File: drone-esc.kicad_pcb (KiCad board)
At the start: 4 copper layers, 34 x 34 mm, 249 parts, among them J1 SM08B-SRSS-TB_LF__SN_, Q1 IRLHS6242, Q10 IRLHS6242, Q11 IRLHS6242, Q12 IRLHS6242, Q13 IRLHS6242, Q14 IRLHS6242, Q15 IRLHS6242, Q16 IRLHS6242, Q17 IRLHS6242, Q18 IRLHS6242, Q19 IRLHS6242, Q2 IRLHS6242, Q20 IRLHS6242, Q21 IRLHS6242, Q22 IRLHS6242, Q23 IRLHS6242, Q24 IRLHS6242, Q3 IRLHS6242, Q4 IRLHS6242, Q5 IRLHS6242, Q6 IRLHS6242, Q7 IRLHS6242, Q8 IRLHS6242, Q9 IRLHS6242, U10 DGD05473FNQ-7, U11 DGD05473FNQ-7, U12 AT32F421G8U7, U13 DGD05473FNQ-7, U14 DGD05473FNQ-7, U15 DGD05473FNQ-7, U16 AT32F421G8U7, U17 DGD05473FNQ-7, U18 DGD05473FNQ-7, U19 DGD05473FNQ-7, U2 INA186A3IDCKR, U20 AT32F421G8U7, U3 TLV76733DRVR, U4 TPS61023DRLR, U5 AT32F421G8U7, U6 DGD05473FNQ-7, U7 DGD05473FNQ-7, U8 DGD05473FNQ-7, U9 DGD05473FNQ-7

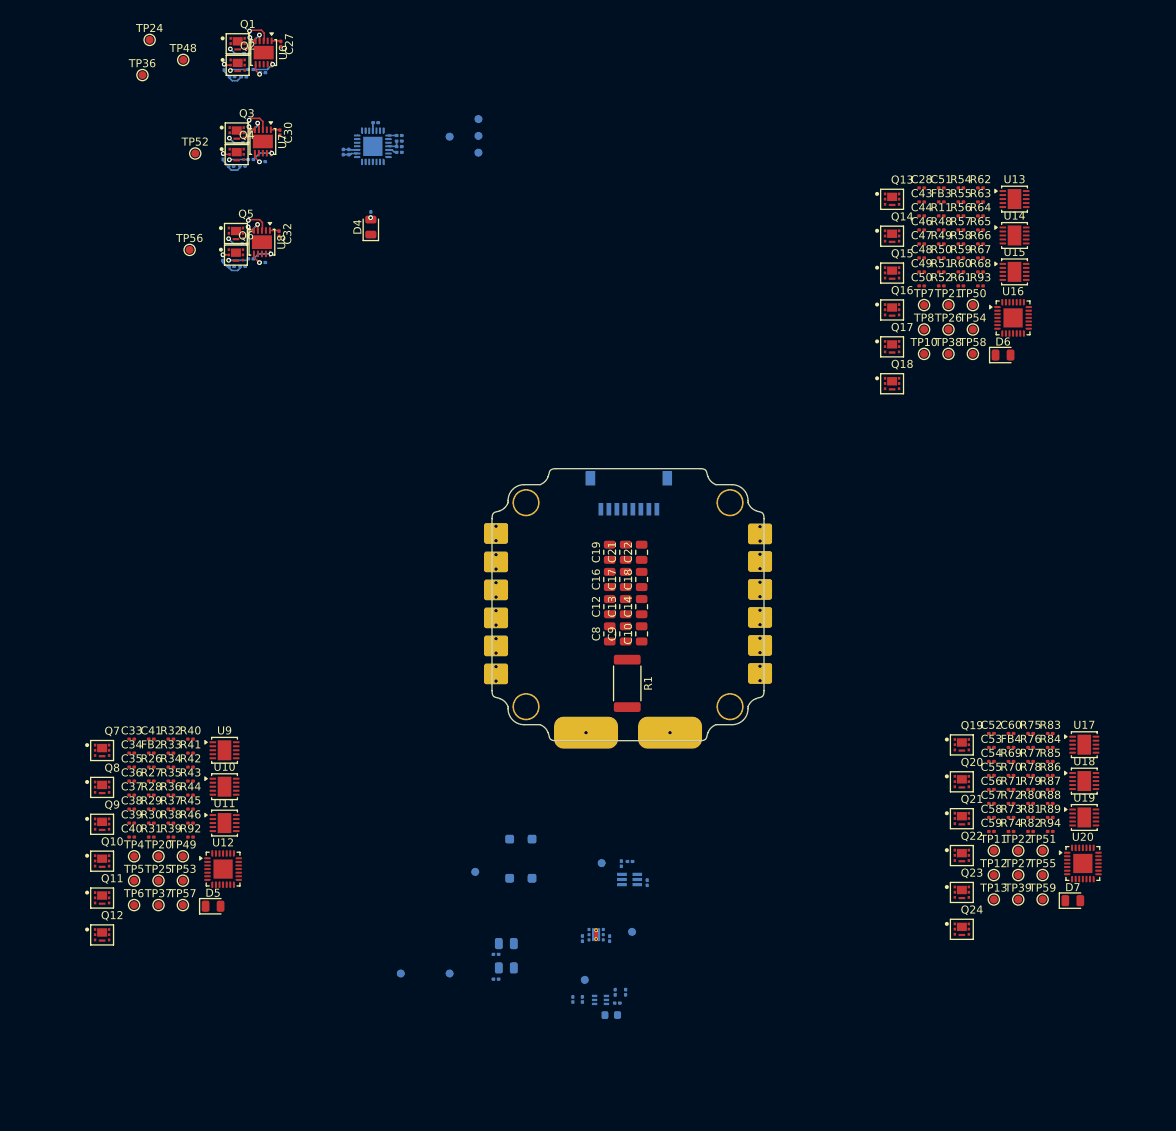
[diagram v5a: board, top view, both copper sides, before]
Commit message: duplicate layout and group
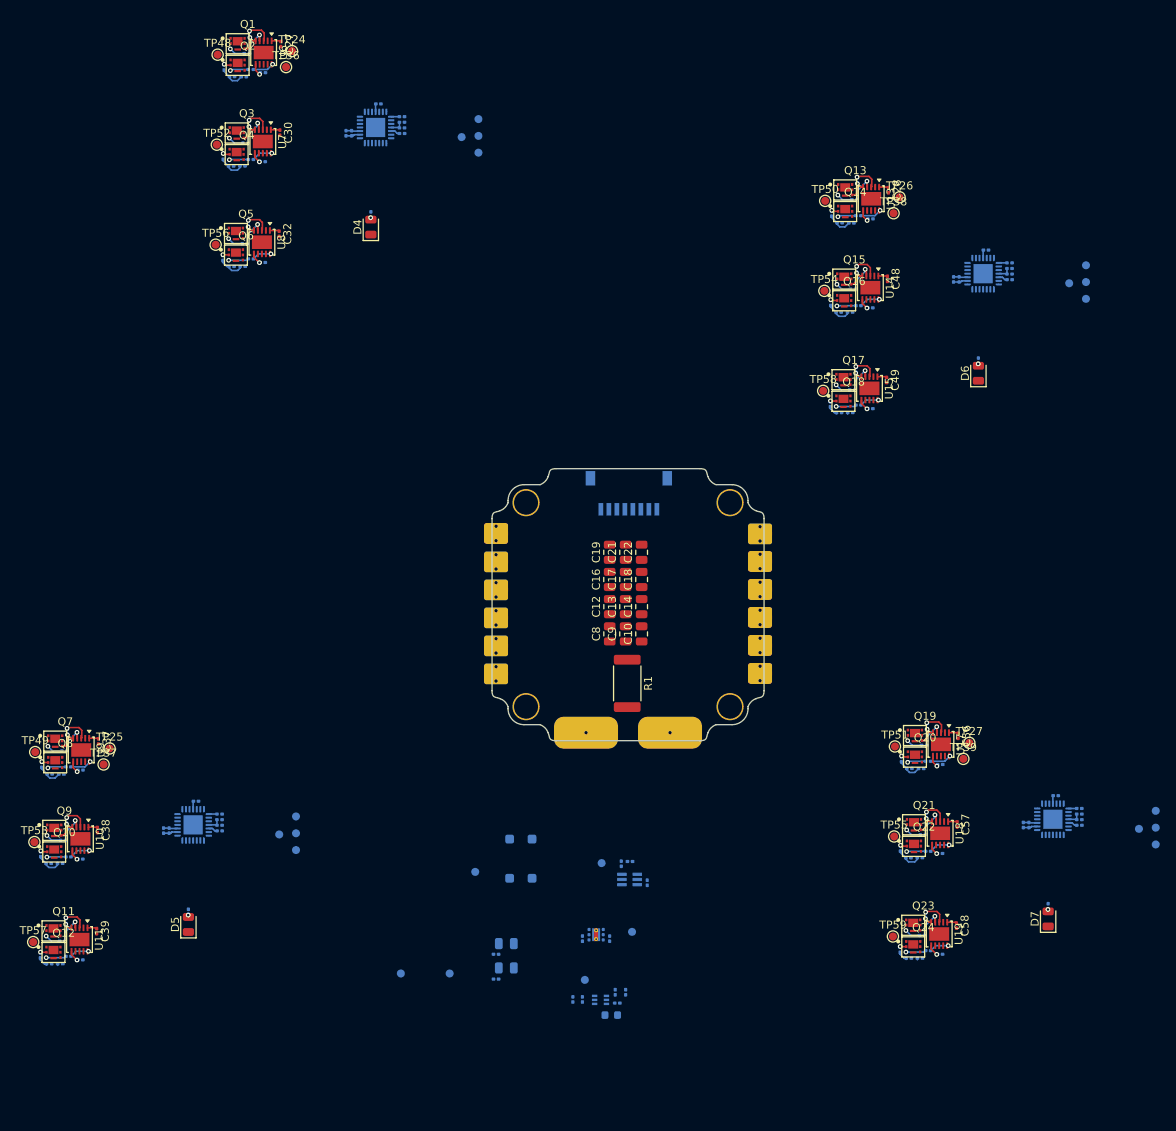
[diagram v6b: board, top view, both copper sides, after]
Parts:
- C33, C34, C35, C36, C40, C41, C43, C44, C46, C47, C50, C51, C52, C53, C54, C55, C59, C60, FB2, FB3, FB4, R11, R26, R27, R28, R29, R30, R31, R32, R33, R34, R35, R36, R37, R38, R39, R40, R41, R42, R43, R44, R45, R46, R48, R49, R50, R51, R52, R54, R55, R56, R57, R58, R59, R60, R61, R62, R63, R64, R65, R66, R67, R68, R69, R70, R71, R72, R73, R74, R75, R76, R77, R78, R79, R80, R81, R82, R83, R84, R85, R86, R87, R88, R89, R92, R93, R94, TP10, TP11, TP12, TP13, TP20, TP21, TP22, TP4, TP5, TP6, TP7, TP8, U12, U16, U20: moved to B.Cu
- moved R42 27.0 mm to (74.3, 137.0), turned to 180 degrees
- moved R85 27.0 mm to (181.7, 136.3), turned to 180 degrees
- moved R64 27.0 mm to (173.0, 68.1), turned to 180 degrees
- moved R86 26.7 mm to (182.5, 138.2), turned to 180 degrees
- moved R43 26.7 mm to (75.0, 138.9), turned to 180 degrees
- moved R65 26.7 mm to (173.8, 70.0), turned to 180 degrees
- moved R87 26.6 mm to (181.5, 139.2), turned to 180 degrees
- moved R66 26.6 mm to (172.8, 71.0), turned to 180 degrees
- moved R44 26.6 mm to (74.0, 139.9), turned to 180 degrees
- moved R45 26.2 mm to (72.6, 139.9)
- moved R67 26.2 mm to (171.4, 71.0)
- moved R88 26.2 mm to (180.1, 139.2)
- moved R46 25.0 mm to (71.5, 138.8), turned to 90 degrees
- moved R68 25.0 mm to (170.3, 69.9), turned to 90 degrees
- moved R89 25.0 mm to (179.0, 138.1), turned to 90 degrees
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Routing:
- net +5V: track 3.52 -> 14.1 mm
- net GND: track 1.81 -> 7.23 mm
- net +3.3V: track 1.77 -> 7.08 mm
- net /ESC4/ESC_EN: track 0.00 -> 4.16 mm, vias 0 -> 3
- net /ESC2/ESC_EN: track 0.00 -> 4.16 mm, vias 0 -> 3
- net /ESC3/ESC_EN: track 0.00 -> 4.16 mm, vias 0 -> 3
- net /ESC2/GATE_B_HIGH: track 0.00 -> 3.87 mm, vias 0 -> 1
- net /ESC4/GATE_B_HIGH: track 0.00 -> 3.87 mm, vias 0 -> 1
- net /ESC3/GATE_B_HIGH: track 0.00 -> 3.87 mm, vias 0 -> 1
- net /ESC4/GATE_C_HIGH: track 0.00 -> 3.71 mm, vias 0 -> 1
- net /ESC2/GATE_C_HIGH: track 0.00 -> 3.71 mm, vias 0 -> 1
- net /ESC3/GATE_C_HIGH: track 0.00 -> 3.71 mm, vias 0 -> 1
- net /ESC4/MotorA: track 0.00 -> 3.63 mm, vias 0 -> 2
- net /ESC2/MotorA: track 0.00 -> 3.63 mm, vias 0 -> 2
- net /ESC3/MotorA: track 0.00 -> 3.63 mm, vias 0 -> 2
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
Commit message: final final group and place
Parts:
- added TP28: 3V3, TestPoint:TestPoint_Pad_D1.0mm, B.Cu at (138.5, 150.7)
- moved C31 27.8 mm to (104.0, 74.4)
- moved Q5 27.8 mm to (102.4, 75.7)
- moved R14 27.8 mm to (104.3, 66.4)
- moved R22 27.8 mm to (100.8, 66.1)
- moved TP24 27.8 mm to (109.4, 52.9)
- moved TP36 27.8 mm to (108.7, 54.9)
- moved C26 27.8 mm to (116.9, 63.1)
- moved C27 27.8 mm to (108.0, 52.0)
- moved C45 27.8 mm to (123.2, 62.5)
- moved D4 27.8 mm to (119.3, 74.9)
- moved FB1 27.8 mm to (123.2, 63.2)
- moved Q3 27.8 mm to (102.5, 63.1)
- moved R12 27.8 mm to (104.3, 55.2)
- moved R15 27.8 mm to (103.5, 76.9)
- moved R16 27.8 mm to (104.3, 78.8)
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
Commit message: good placement 1
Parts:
- removed the D1 at (145.1, 146.0)
- removed TP48, TP49, TP50, TP51: MOTORA, TestPoint:TestPoint_Pad_D1.0mm
- removed TP52, TP53, TP54, TP55: MOTORB, TestPoint:TestPoint_Pad_D1.0mm
- removed TP56, TP57, TP58, TP59: MOTORC, TestPoint:TestPoint_Pad_D1.0mm
- R17, R19: moved to F.Cu
- moved R19 3.64 mm to (105.5, 55.6), turned to 180 degrees
- moved R17 3.60 mm to (107.0, 55.6)
- moved C42 2.19 mm to (105.4, 52.5), turned to 180 degrees
- moved R8 1.72 mm to (104.9, 54.1), turned to 90 degrees
- moved R53 1.47 mm to (103.8, 51.7)
- moved R18 0.56 mm to (101.4, 54.6), turned to 0 degrees
- moved R27 0.19 mm to (102.3, 112.3)
- moved R11 0.19 mm to (181.1, 61.4)
- moved R70 0.19 mm to (184.1, 115.2)
- moved TP36 0.12 mm to (108.7, 54.8)
- moved TP24 0.07 mm to (109.4, 52.8)
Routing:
- net /ESC1/FBA: track 3.08 -> 6.85 mm, vias 0 -> 2
- net /ESC1/MotorA: track 3.63 -> 1.04 mm
- net Net-(U6-VB): track 3.04 -> 1.02 mm
- net /ESC1/GATE_A_HIGH: track 3.58 -> 1.80 mm
- net /ESC1/ESC_EN: track 4.16 -> 2.81 mm
